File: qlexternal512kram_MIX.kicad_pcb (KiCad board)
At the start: 2 copper layers, 97.8 x 35.6 mm, 15 parts, among them J1 QL_SLOT_DIN41612_CARD, J2 QL_SLOT_DIN41612_CARD, U1 HM628512BLFP-7, U2 GAL16V8B-25QP, U3 LM1117-5.0

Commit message: modifying it
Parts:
- moved C1 2.94 mm to (99.0, 70.8), turned to 180 degrees
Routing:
- net GND: track 228.6 -> 78.7 mm, vias 0 -> 14
- net /DTACK: track 76.8 -> 38.2 mm, vias 1 -> 5
- net +9V: track 48.4 -> 32.0 mm
- net /D5: track 99.2 -> 86.9 mm, vias 0 -> 3
- net /A15: track 87.2 -> 74.9 mm
- net /A3: track 59.8 -> 48.4 mm, vias 0 -> 1
- net /A2: track 59.8 -> 51.9 mm, vias 0 -> 1
- net /AS: track 69.7 -> 63.4 mm, vias 1 -> 3
- net /A1: track 54.6 -> 51.0 mm, vias 0 -> 1
- net /D4: track 77.0 -> 79.1 mm
- net /A12: track 44.0 -> 41.9 mm, vias 0 -> 1
- net /D3: track 69.1 -> 67.2 mm
- net /DSMC: track 121.1 -> 122.4 mm
- net VCC: track 100.6 -> 99.5 mm
- net /D0: track 60.0 -> 60.5 mm, vias 0 -> 1
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- added copper zone on B.Cu, net GND
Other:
- board size 97.8 x 35.6 mm -> 97.8 x 36.3 mm
- board text added: "Modified by Popopo"
- board text removed: "By Alvaro Alea Fdz."
- board text removed: "www.va-de-retro.com"

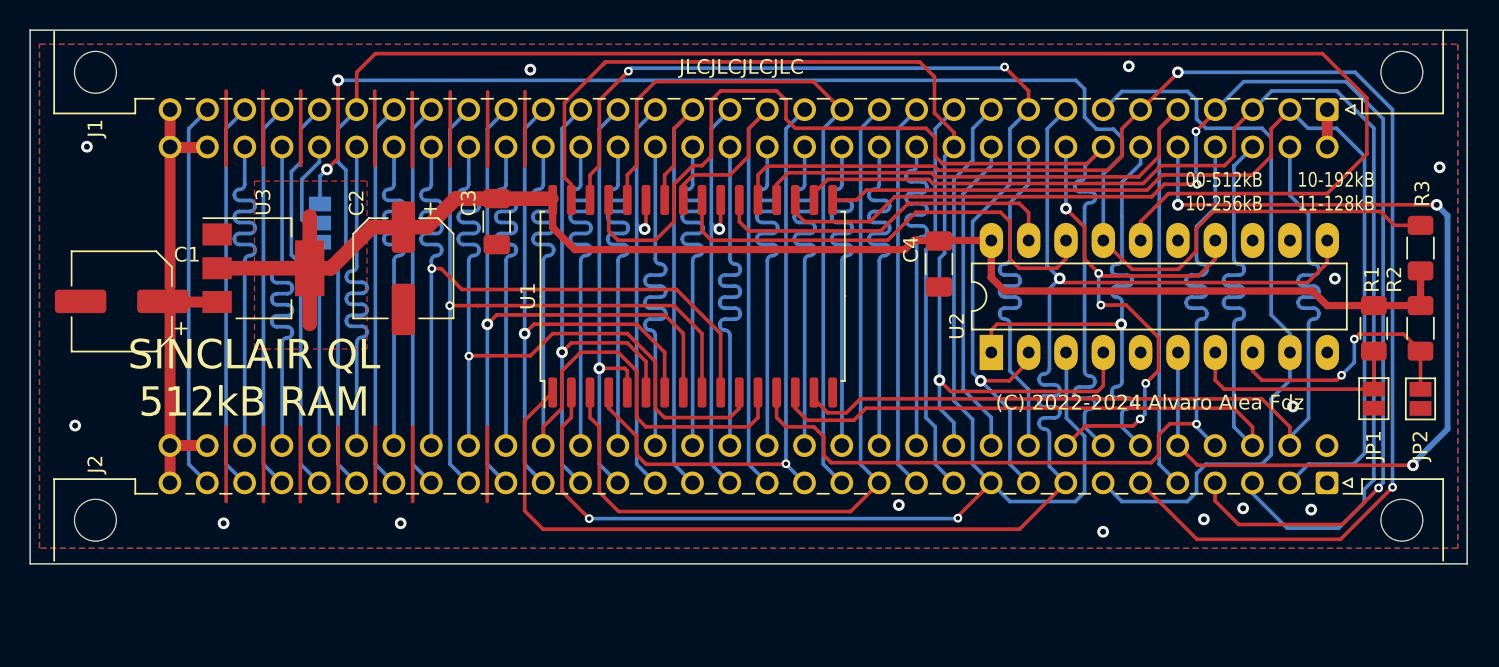
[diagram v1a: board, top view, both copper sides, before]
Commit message: Changing PCB size and components orientation
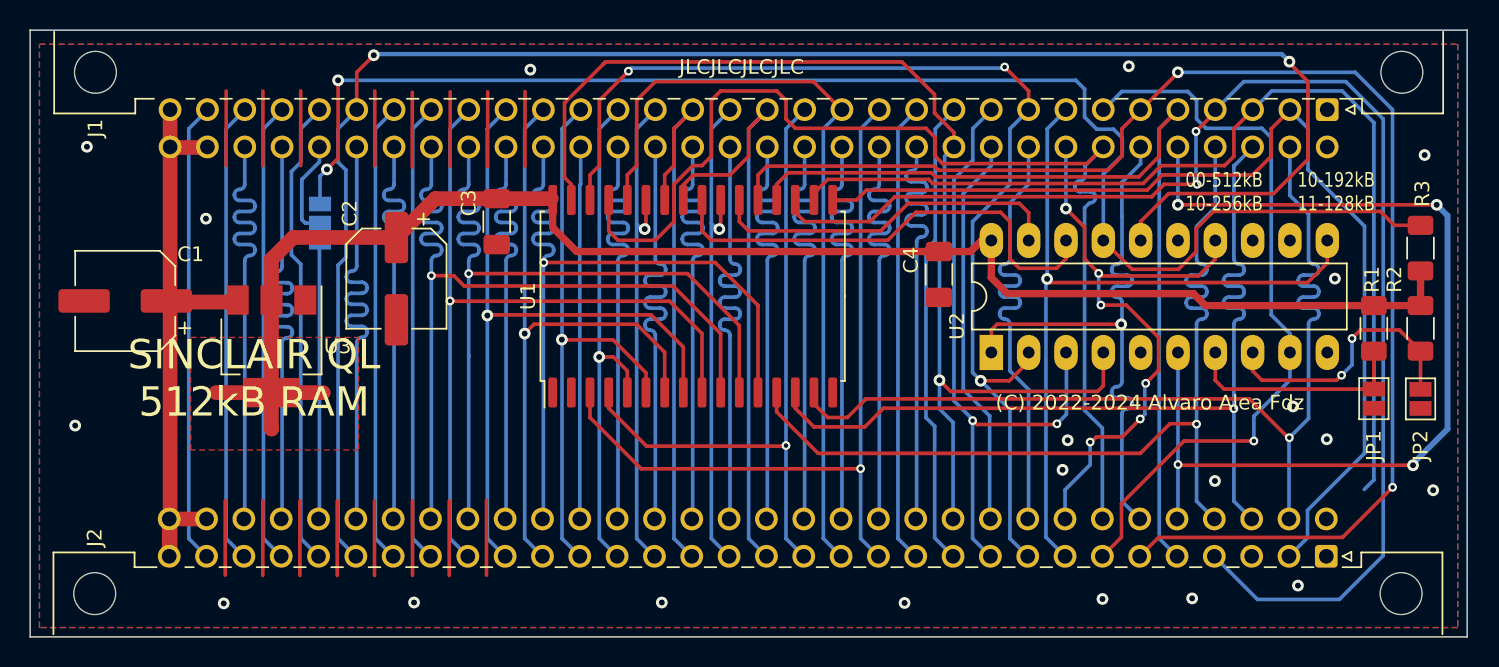
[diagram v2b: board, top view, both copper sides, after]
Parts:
- moved U3 5.34 mm to (109.2, 73.9), turned to -90 degrees
- moved J2 5.00 mm to (181.0, 88.2)
- moved C2 0.85 mm to (117.7, 69.3)
- moved C4 0.72 mm to (154.7, 69.0)
- moved C1 0.24 mm to (99.3, 70.8)
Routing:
- net /A18: track 99.9 -> 52.7 mm
- net /A16: track 82.7 -> 43.4 mm
- net /D4: track 79.1 -> 68.4 mm
- net +9V: track 32.0 -> 41.0 mm
- net VCC: track 99.5 -> 107.2 mm
- net /A7: track 29.9 -> 35.2 mm
- net /A3: track 48.4 -> 53.5 mm
- net /VSYNC: track 26.4 -> 31.4 mm
- net /ROMOE: track 26.4 -> 31.4 mm
- net /RESET: track 26.4 -> 31.4 mm
- net /E: track 26.4 -> 31.4 mm
- net /CSYNC: track 26.4 -> 31.4 mm
- net /BG: track 26.4 -> 31.4 mm
- net /VPA: track 26.4 -> 31.4 mm
- net /IPL1: track 26.4 -> 31.4 mm
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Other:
- board size 97.8 x 36.3 mm -> 97.8 x 41.3 mm

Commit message: version pre-release 1
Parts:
- removed JP1, JP2: Jumper_2_Open, Jumper:SolderJumper-2_P1.3mm_Open_Pad1.0x1.5mm
- removed JP3: Jumper_3_Open, Jumper:SolderJumper-3_P1.3mm_Open_Pad1.0x1.5mm
- added REF**: KiCad-Logo2_5mm_SilkScreen, Symbol:KiCad-Logo2_5mm_SilkScreen, B.Cu at (101.8, 67.3)
- added REF**: Symbol_Attention_Triangle_8x7mm_Copper, Symbol:Symbol_Attention_Triangle_8x7mm_Copper, B.Cu at (115.6, 77.7)
- added REF**: OSHW-Logo_5.7x6mm_SilkScreen, Symbol:OSHW-Logo_5.7x6mm_SilkScreen, B.Cu at (101.7, 74.0)
- added SW1: SW_DIP_x02, Button_Switch_SMD:SW_DIP_SPSTx02_Slide_KingTek_DSHP02TS_W7.62mm_P1.27mm, F.Cu at (186.6, 76.1)
- added SW2: SW_SPDT, Button_Switch_SMD:SW_SPDT_PCM12, F.Cu at (111.5, 65.8)
- moved R3 69.2 mm to (118.3, 65.6)
- moved C2 10.4 mm to (121.3, 79.0), turned to 0 degrees
- moved C1 8.26 mm to (97.9, 78.9), turned to -90 degrees
- moved R1 5.90 mm to (185.6, 66.9)
- moved R2 5.78 mm to (188.0, 66.9)
- moved U3 2.12 mm to (108.6, 75.9), turned to 0 degrees
- moved C4 0.33 mm to (154.9, 69.2)
- moved C3 0.07 mm to (124.6, 65.5)
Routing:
- net /A18: track 52.7 -> 99.6 mm
- net /A16: track 43.4 -> 75.0 mm, vias 2 -> 3
- net Net-(SW2-C): track 97.9 -> 78.0 mm, vias 2 -> 1
- net GND: track 81.3 -> 96.6 mm, vias 20 -> 46
- net /D4: track 68.4 -> 79.3 mm, vias 0 -> 2
- net /A0: track 53.1 -> 44.3 mm
- net /A1: track 55.9 -> 47.7 mm
- net /A2: track 56.7 -> 48.7 mm
- net VCC: track 107.2 -> 114.6 mm
- net /VSYNC: track 31.4 -> 25.3 mm
- net /FC2: track 31.4 -> 25.3 mm
- net /GREEN: track 31.4 -> 25.3 mm
- net /IPL0: track 31.4 -> 25.3 mm
- net /VPA: track 31.4 -> 25.3 mm
- net /FC1: track 31.4 -> 25.3 mm
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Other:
- board text added: "0"
- board text added: "1"
- board text added: "1 2 3"
- board text added: "NOTE SW2: 1-2 Default Position 2-3 For use as +256Kb with Alvaro's Trump Card Install the +256K expansion after Alvaro's Trump Card"
- board text added: "Original Author: Alvaro Alea Fdz"
- board text added: "REV.1"
- board text added: "SINCLAIR QL 512KB RAM"
- board text added: "WARNING: Use it under your own risk. Combining this card with others without a proper Switches configuration may result in damage for your QL. Install it only with QL unplugged from power."
- board text removed: "(C) 2022-2024 Alvaro Alea Fdz"
- board text removed: "REV.3"
- board text removed: "SINCLAIR QL 512kB RAM"

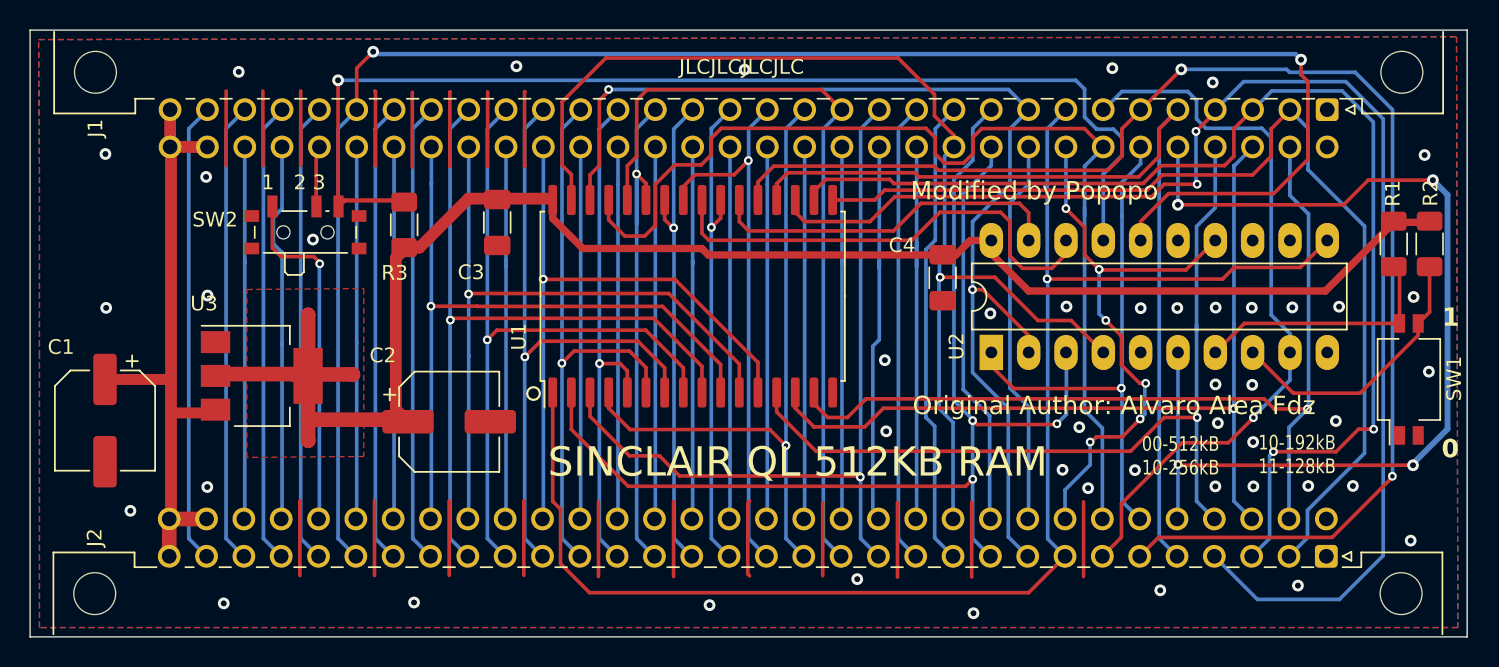
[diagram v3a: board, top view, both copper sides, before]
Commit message: added labels
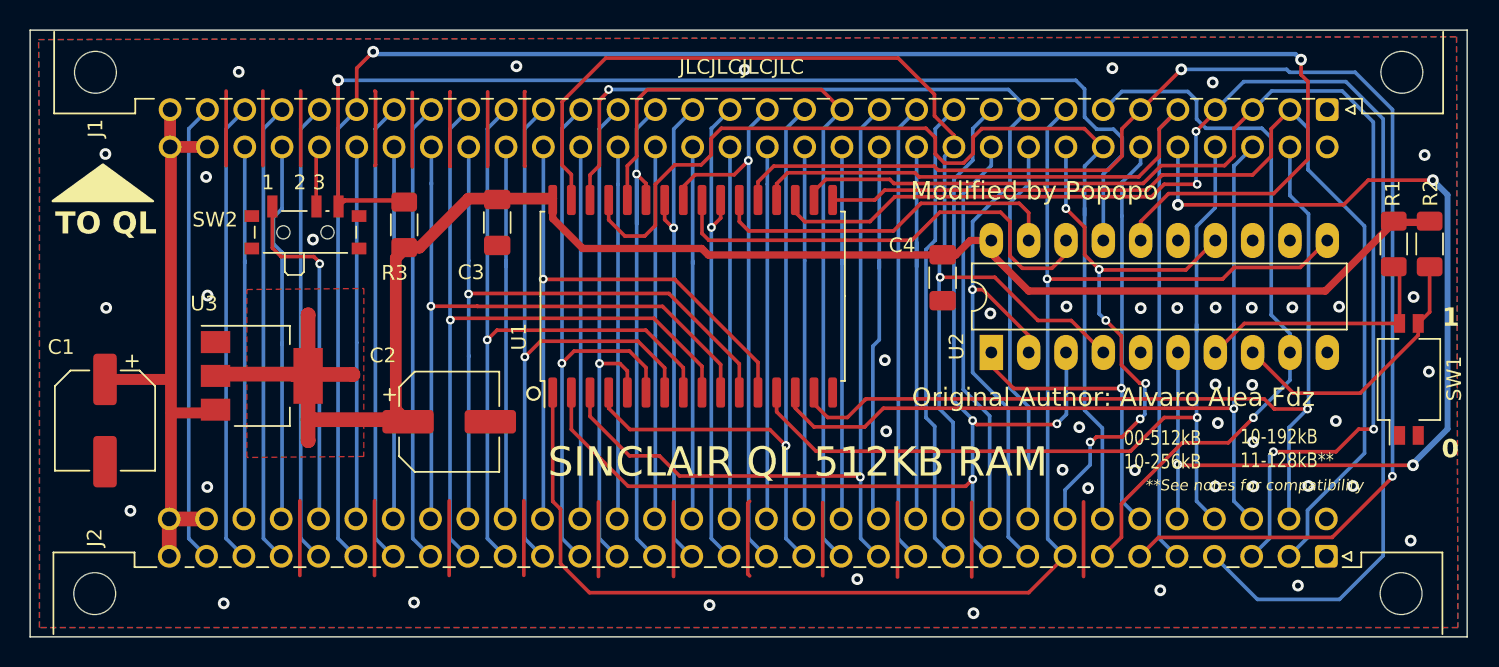
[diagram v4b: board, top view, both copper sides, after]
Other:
- board text added: "**See notes for compatibility"
- board text added: "10-192kB 11-128kB**"
- board text added: "Bottom Side"
- board text added: "TO QL"
- board text removed: "10-192kB 11-128kB"
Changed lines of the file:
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@@
 		)
 		(property "Value" "LM1117-5.0"
-			(at 0 4.5 360)
+			(at 0 4.5 0)
 			(layer "F.Fab")
 			(effects
@@
 		)
 		(property "Footprint" "Package_TO_SOT_SMD:SOT-223-3_TabPin2"
-			(at 0 0 360)
+			(at 0 0 0)
 			(layer "F.Fab")
 			(hide yes)
@@
 		)
 		(property "Datasheet" "http://www.ti.com/lit/ds/symlink/lm1117.pdf"
-			(at 0 0 360)
+			(at 0 0 0)
 			(layer "F.Fab")
 			(hide yes)
@@
 		)
 		(property "Description" ""
-			(at 0 0 360)
+			(at 0 0 0)
 			(layer "F.Fab")
 			(hide yes)
@@
 		(tags "capacitor electrolytic")
 		(property "Reference" "C2"
-			(at -4.51 -4.51 360)
+			(at -4.51 -4.51 0)
 			(layer "F.SilkS")
 			(effects
@@
 		)
 		(property "Value" "100u/16V"
-			(at 0 4.35 360)
+			(at 0 4.35 0)
 			(layer "F.Fab")
 			(effects
@@
 		)
 		(property "Footprint" "Capacitor_SMD:CP_Elec_6.3x5.4"
-			(at 0 0 360)
+			(at 0 0 0)
 			(layer "F.Fab")
 			(hide yes)
@@
 		)
 		(property "Datasheet" ""
-			(at 0 0 360)
+			(at 0 0 0)
 			(layer "F.Fab")
 			(hide yes)
@@
 		)
 		(property "Description" ""
-			(at 0 0 360)
+			(at 0 0 0)
 			(layer "F.Fab")
 			(hide yes)
@@
 		)
 		(fp_text user "${REFERENCE}"
-			(at 0 0 360)
+			(at 0 0 0)
 			(layer "F.Fab")
 			(effects
@@
 		(layer "F.SilkS")
 	)
+	(gr_poly
+		(pts
+			(xy 94.34 64.015) (xy 101.17 64.015) (xy 97.76 61.515) (xy 94.35 63.995)
+		)
+		(stroke
+			(width 0.15)
+			(type solid)
+		)
+		(fill solid)
+		(layer "F.SilkS")
+	)
 	(gr_rect
 		(start 92.805 52.375)
@@
 		)
 	)
+	(gr_text "Bottom Side"
+		(at 172.53 81.255 0)
+		(layer "B.SilkS")
+		(effects
+			(font
+				(size 2 2)
+				(thickness 0.25)
+				(bold yes)
+			)
+			(justify bottom mirror)
+		)
+	)
 	(gr_text "REV.1"
 		(at 112.37 91.215 0)
@@
 		)
 	)
+	(gr_text "TO QL"
+		(at 94.5 66.395 0)
+		(layer "F.SilkS")
+		(effects
+			(font
+				(size 1.5 1.5)
+				(thickness 0.2)
+				(bold yes)
+			)
+			(justify left bottom)
+		)
+	)
 	(gr_text "JLCJLCJLCJLC"
 		(at 141.22 54.885 0)
@@
 		)
 	)
-	(gr_text "10-192kB\n11-128kB "
-		(at 176.38 81.255 0)
+	(gr_text "**See notes for compatibility\n"
+		(at 168.66 83.785 0)
+		(layer "F.SilkS")
+		(effects
+			(font
+				(size 0.75 0.75)
+				(thickness 0.15)
+				(italic yes)
+			)
+			(justify left bottom)
+		)
+	)
+	(gr_text "10-192kB\n11-128kB** "
+		(at 175.15 80.845 0)
 		(layer "F.SilkS")
 		(effects
@@
 	)
 	(gr_text "Original Author: Alvaro Alea Fdz"
-		(at 166.57 77.925 0)
+		(at 166.52 77.365 0)
 		(layer "F.SilkS")
 		(effects
@@
 	)
 	(gr_text "00-512kB\n10-256kB"
-		(at 168.46 81.345 0)
+		(at 167.23 80.935 0)
 		(layer "F.SilkS")
 		(effects

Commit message: produced Gerber vers 1a
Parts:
- C1, C2: footprint Capacitor_SMD:CP_Elec_6.3x5.4 -> Library:CP_Elec_6.3x5.4_Long_Pad
- REF**: footprint Symbol:Symbol_Attention_Triangle_8x7mm_Copper -> Library:Symbol_Attention_Triangle_8x7mm_Copper
- SW2: footprint Button_Switch_SMD:SW_SPDT_PCM12 -> Library:SW_SPDT_PCM12
- U3: footprint Package_TO_SOT_SMD:SOT-223-3_TabPin2 -> Library:SOT-223-3_TabPin2_Long_Pads
- moved R3 2.13 mm to (119.4, 63.8), turned to 180 degrees
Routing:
- net /AS: track 70.1 -> 68.9 mm
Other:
- board text added: "00-512kB 01-256kB"
- board text removed: "00-512kB 10-256kB"

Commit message: updating schema and symbols
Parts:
- J2: footprint 8bits:DIN41612_B_2x32_Male_Horizontal_THT -> Library:DIN41612_B_2x32_Male_Horizontal_THT
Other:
- board size 97.8 x 41.3 mm -> 97.8 x 40.9 mm
